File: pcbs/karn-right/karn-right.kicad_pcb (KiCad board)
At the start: 2 copper layers, 46 parts, among them SW11 SW_Push, SW12 SW_Push, SW13 SW_Push, SW14 SW_Push, SW15 SW_Push, SW21 SW_Push, SW22 SW_Push, SW23 SW_Push, SW24 SW_Push, SW25 SW_Push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

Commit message: Various changes:
- Add start of parts list
- Fix impossible placement of diodes
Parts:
- removed Bat+1, BatGND1: MountingHole_Pad, kbd:1pin_conn
- added J1: S2B-PH-K-SLFSN, kbd:S2B-PH-K-SLFSN, F.Cu at (79.4, 79.0)
- moved L1 116.5 mm to (178.0, 40.0)
- moved L2 116.5 mm to (184.0, 40.0)
- moved L3 116.5 mm to (190.0, 40.0)
- moved SW_POWER1 37.0 mm to (67.0, 70.5), turned to -90 degrees
- moved D41 15.7 mm to (63.0, 106.0)
- moved D43 15.0 mm to (106.5, 88.0)
- moved D42 14.9 mm to (82.5, 94.0)
- moved D31 13.8 mm to (82.8, 79.0), turned to -90 degrees
- moved D34 13.8 mm to (138.2, 79.0), turned to 90 degrees
- moved D33 13.3 mm to (119.8, 79.0), turned to 90 degrees
- moved D35 13.3 mm to (156.8, 79.0), turned to 90 degrees
- moved D32 13.2 mm to (101.2, 79.0), turned to -90 degrees
- moved D15 10.6 mm to (161.0, 48.8)
- moved D24 10.6 mm to (142.5, 66.2)
- moved D12 10.4 mm to (105.5, 48.8)
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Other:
- board text added: "BATTERY"

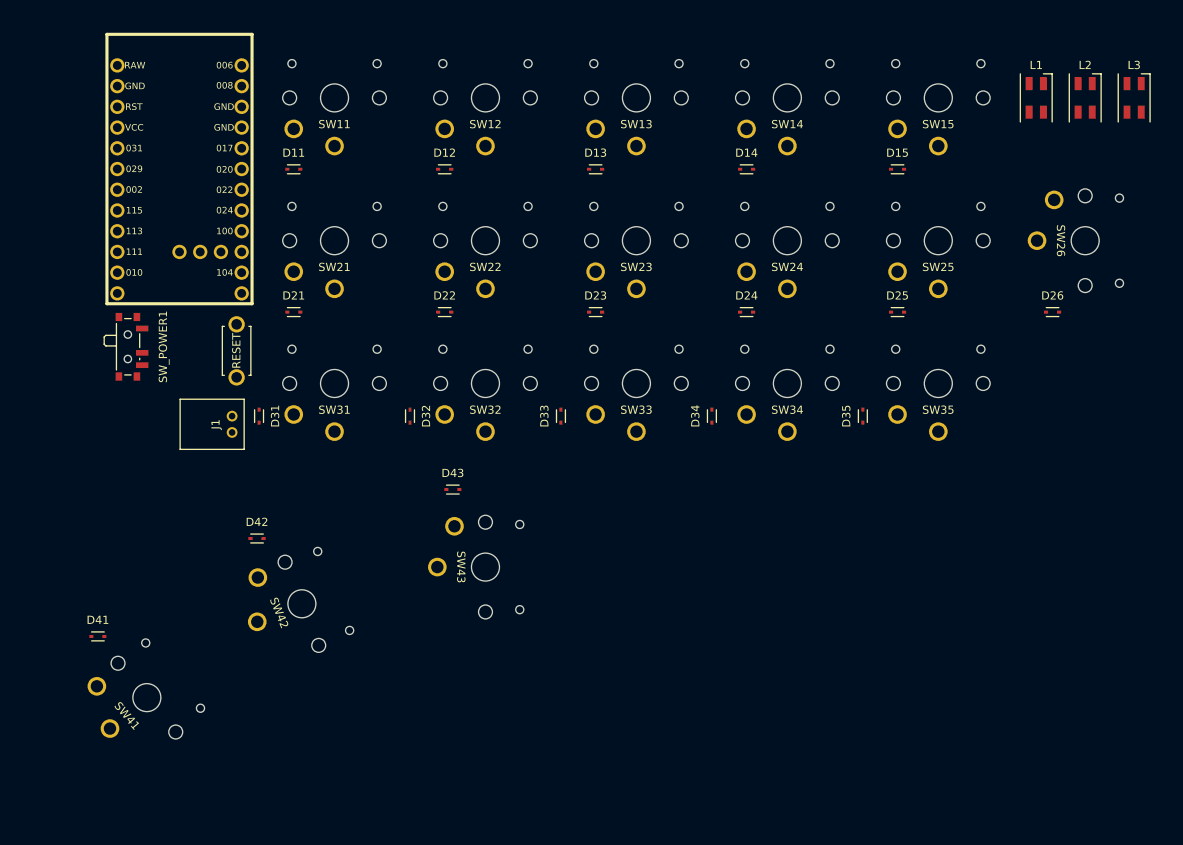
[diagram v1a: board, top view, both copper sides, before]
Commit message: Add first draft of routing
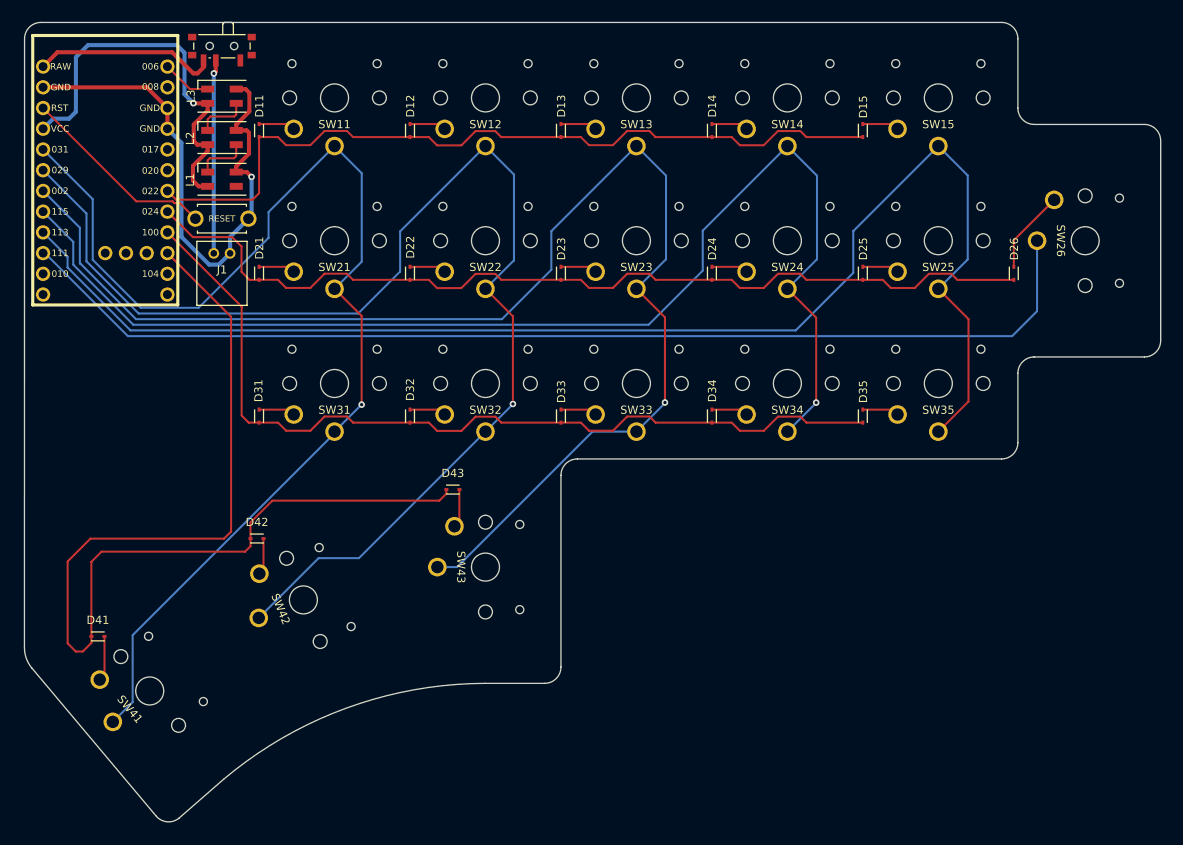
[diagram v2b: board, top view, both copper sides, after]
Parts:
- moved L3 111.8 mm to (78.2, 39.8), turned to 180 degrees
- moved L2 105.9 mm to (78.2, 44.9), turned to 180 degrees
- moved L1 100.3 mm to (78.2, 50.0), turned to 180 degrees
- moved SW_POWER1 38.2 mm to (78.2, 34.0), turned to 180 degrees
- moved J1 20.1 mm to (77.2, 59.1), turned to 0 degrees
- moved RSW1 16.3 mm to (78.2, 54.8), turned to 0 degrees
- moved U1 9.10 mm to (63.9, 50.1)
- moved D26 6.72 mm to (175.2, 61.5), turned to 90 degrees
- moved D11 6.37 mm to (82.8, 44.0), turned to 90 degrees
- moved D12 6.37 mm to (101.2, 44.0), turned to 90 degrees
- moved D13 6.37 mm to (119.8, 44.0), turned to 90 degrees
- moved D14 6.37 mm to (138.2, 44.0), turned to 90 degrees
- moved D15 6.37 mm to (156.8, 44.0), turned to 90 degrees
- moved D21 6.37 mm to (82.8, 61.5), turned to 90 degrees
- moved D22 6.37 mm to (101.2, 61.5), turned to 90 degrees
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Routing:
- net col5: track 0.00 -> 168.9 mm
- net col3: track 0.00 -> 165.5 mm, vias 0 -> 1
- net col2: track 0.00 -> 154.2 mm, vias 0 -> 1
- net col4: track 0.00 -> 151.5 mm, vias 0 -> 1
- net col1: track 0.00 -> 145.5 mm, vias 0 -> 1
- net col6: track 0.00 -> 135.9 mm
- net row4: track 0.00 -> 131.8 mm
- net row2: track 0.00 -> 116.2 mm
- net row3: track 0.00 -> 108.5 mm
- net row1: track 0.00 -> 98.7 mm
- net GND: track 0.00 -> 67.5 mm, vias 0 -> 1
- net VCC: track 0.00 -> 48.7 mm, vias 0 -> 1
- net reset: track 0.00 -> 24.3 mm
- net BT+: track 0.00 -> 23.8 mm, vias 0 -> 1
- net raw: track 0.00 -> 22.6 mm
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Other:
- board outline added: 139.3 x 98 mm

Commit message: Add gnd planes
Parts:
- J1: value S2B-PH-K-SLFSN -> CONN_S2B-PH-K-S_JST
- moved SW_POWER1 0.19 mm to (78.2, 34.2)
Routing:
- added copper zone on B.Cu, net GND
- added copper zone on F.Cu, net GND
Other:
- board text added: "robcmills/karn-keyboard"

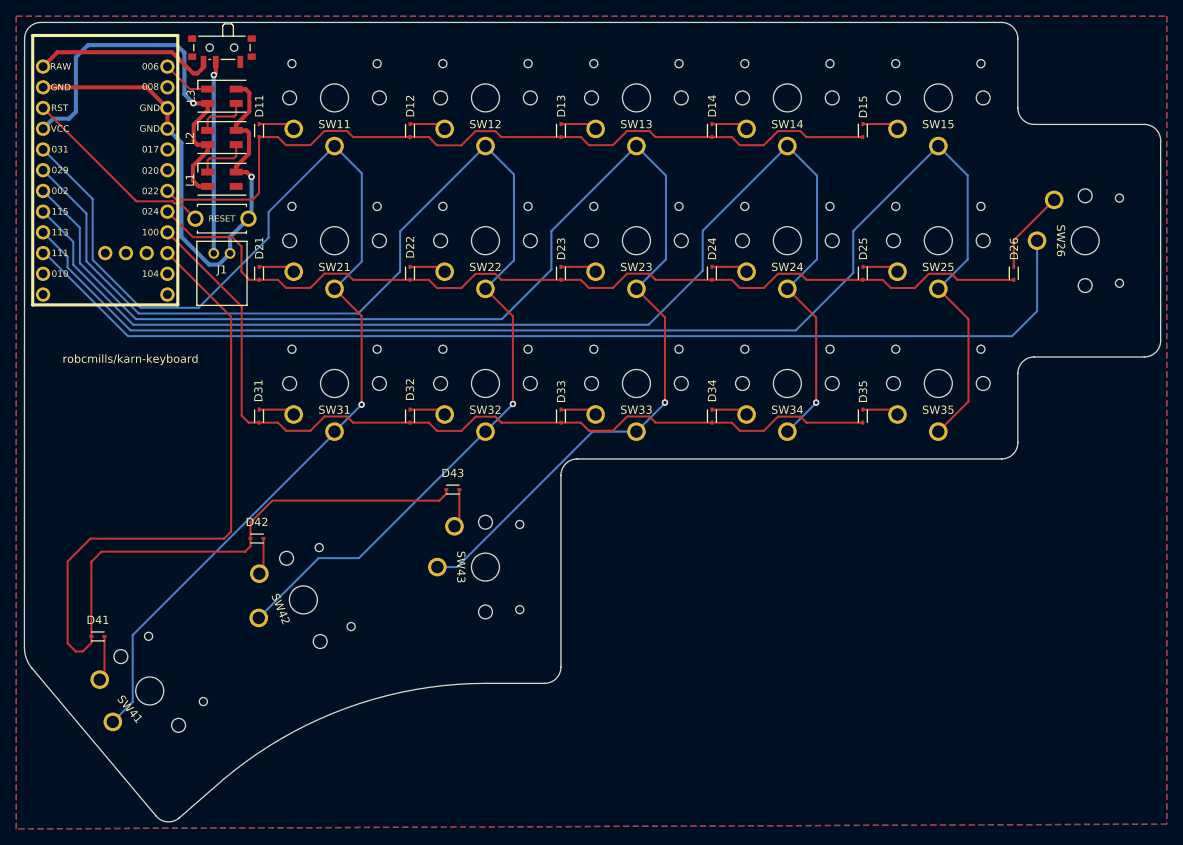
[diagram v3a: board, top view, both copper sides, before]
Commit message: karn-right v1 with gerber files
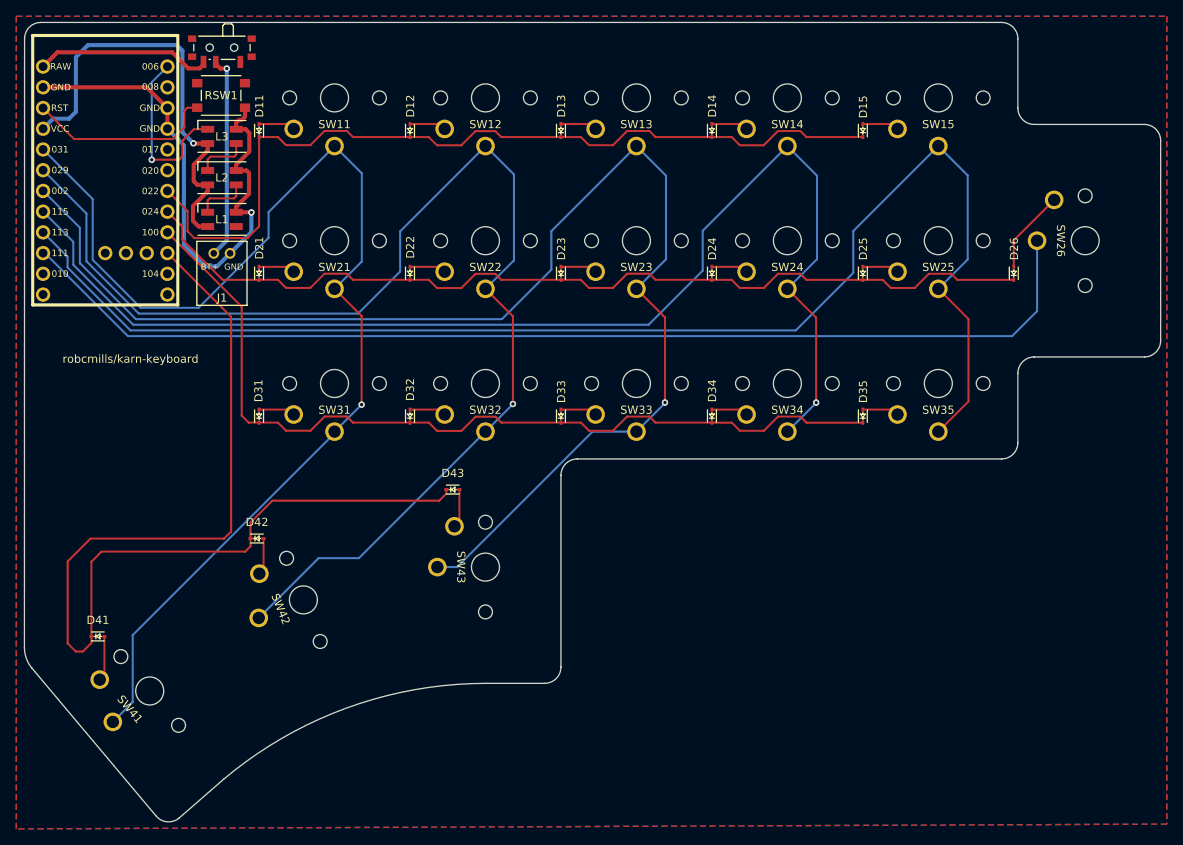
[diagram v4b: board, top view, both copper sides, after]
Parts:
- J1: value CONN_S2B-PH-K-S_JST -> S2B-PH-K-SLFSN
- RSW1: footprint kbd:ResetSW -> karn-kicad-footprints:reset-switch-TL3313AF250QG
- moved RSW1 15.1 mm to (78.1, 39.7)
- moved L1 4.92 mm to (78.2, 54.9)
- moved L2 4.92 mm to (78.2, 49.8)
- moved L3 4.92 mm to (78.2, 44.7)
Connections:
- RSW1 pad 1: GND -> unconnected-(RSW1-Pad1)
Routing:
- net led: track 6.07 -> 21.7 mm, vias 0 -> 1
- net row1: track 98.7 -> 106.4 mm
- net VCC: track 48.7 -> 53.7 mm
- net BT+: track 23.6 -> 25.1 mm
- net reset: track 24.3 -> 23.2 mm
- net raw: track 22.6 -> 21.7 mm
- net row2: track 116.2 -> 115.3 mm
- net GND: track 67.5 -> 66.8 mm

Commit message: Various changes:
- Fix incorrect reset-switch-TL3313 symbol and footprint
- Increase size of diode footprint pads
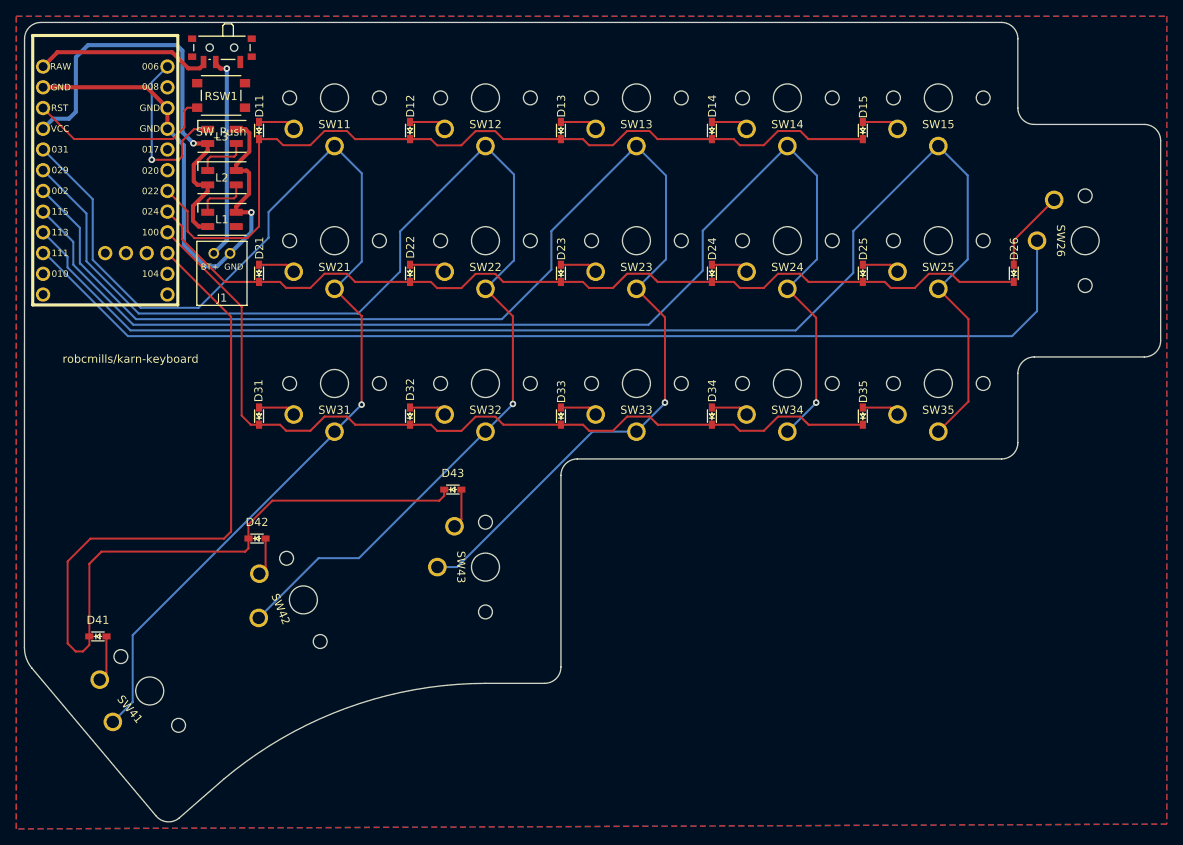
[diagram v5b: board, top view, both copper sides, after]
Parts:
- RSW1: footprint karn-kicad-footprints:reset-switch-TL3313AF250QG -> karn-kicad:reset-switch-TL3313AF250QG
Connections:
- RSW1 pad 1: unconnected-(RSW1-Pad1) -> reset
- RSW1 pad 2: reset -> unconnected-(RSW1-Pad2)
- RSW1 pad 4: unconnected-(RSW1-Pad4) -> GND
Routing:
- net GND: track 66.8 -> 63.5 mm
